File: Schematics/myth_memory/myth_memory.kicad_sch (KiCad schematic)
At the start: 6 parts, among them U1 74HC04, U3 SST39SF040, U4 74LS32, U5 74LS21, U6 4002, U94 KM62256CLP

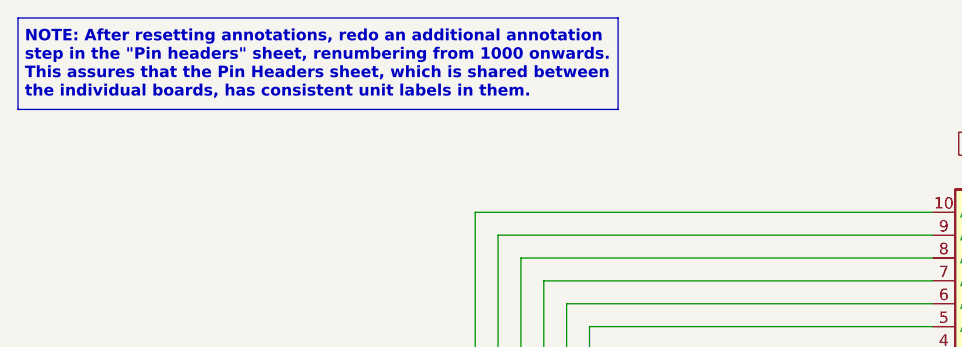
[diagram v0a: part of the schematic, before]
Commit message: Reduce number of shared headers
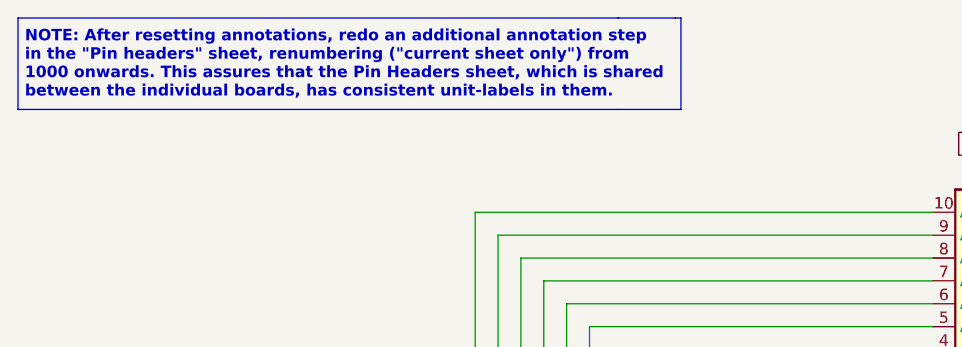
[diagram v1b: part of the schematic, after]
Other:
- note added: "NOTE: After resetting annotations, redo an additional annotation step in the "Pin headers" sheet, renumbering ("current sheet only") from 1000 onwards. This assures that the Pin Headers sheet, which is shared between the individual boards, has consistent unit-labels in them."
- note removed: "NOTE: After resetting annotations, redo an additional annotation step in the "Pin headers" sheet, renumbering from 1000 onwards. This assures that the Pin Headers sheet, which is shared between the individual boards, has consistent unit labels in them."

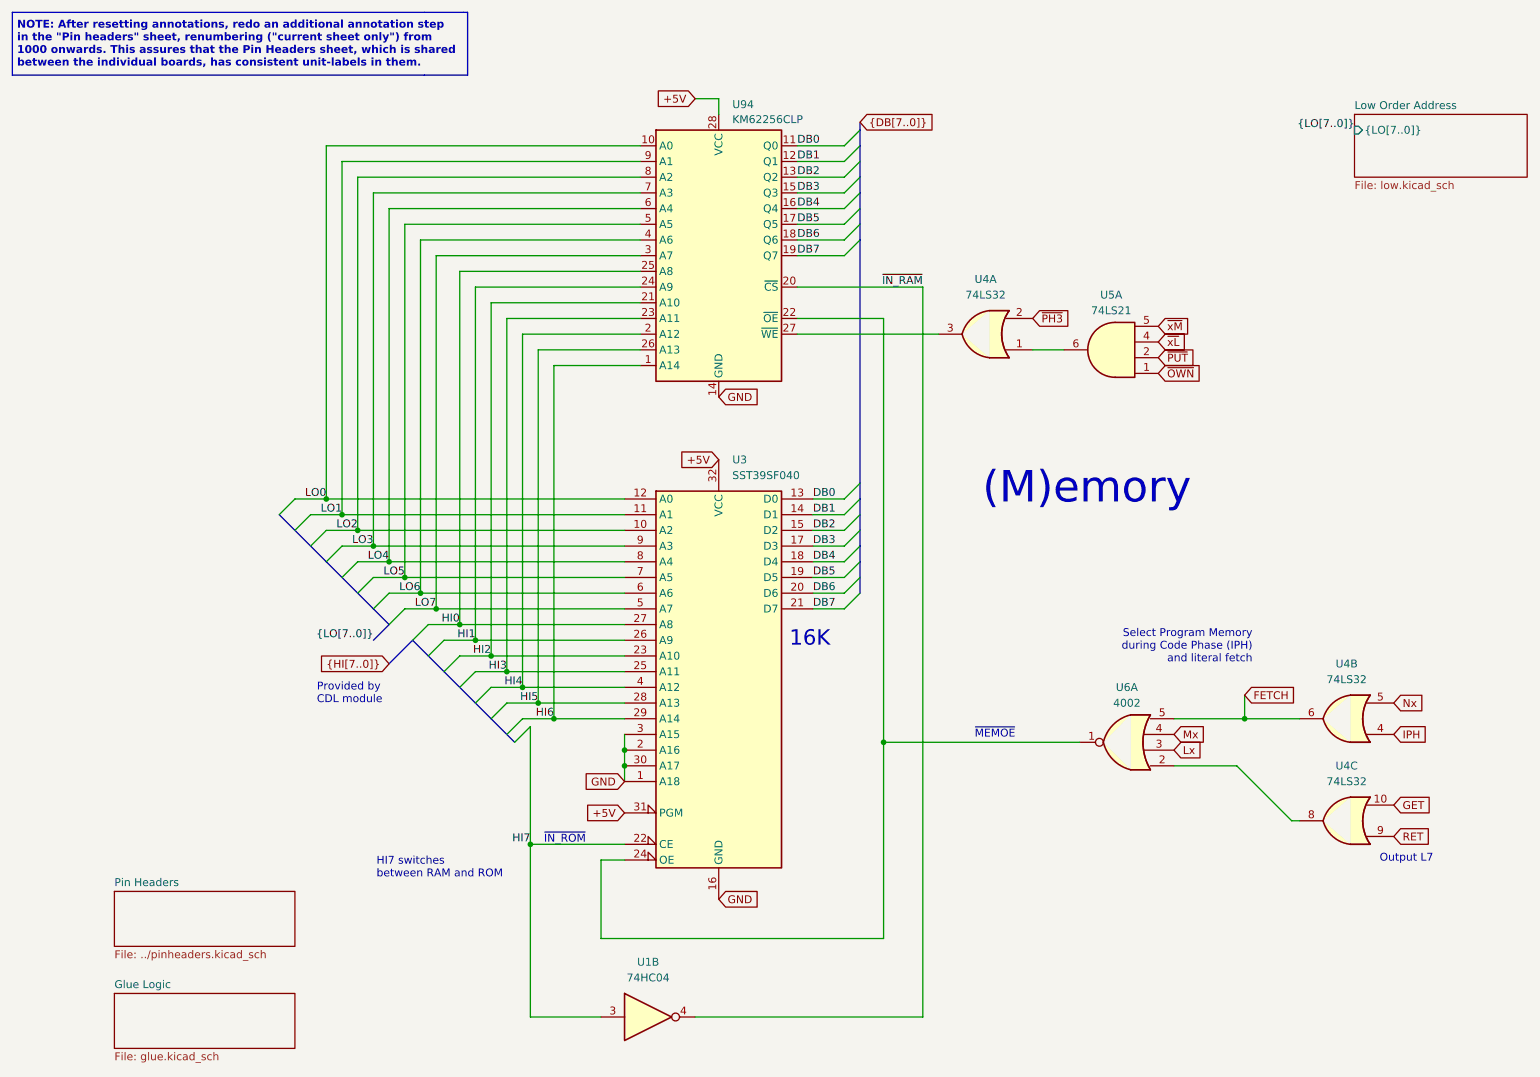
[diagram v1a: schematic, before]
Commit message: Improve schematics for readability
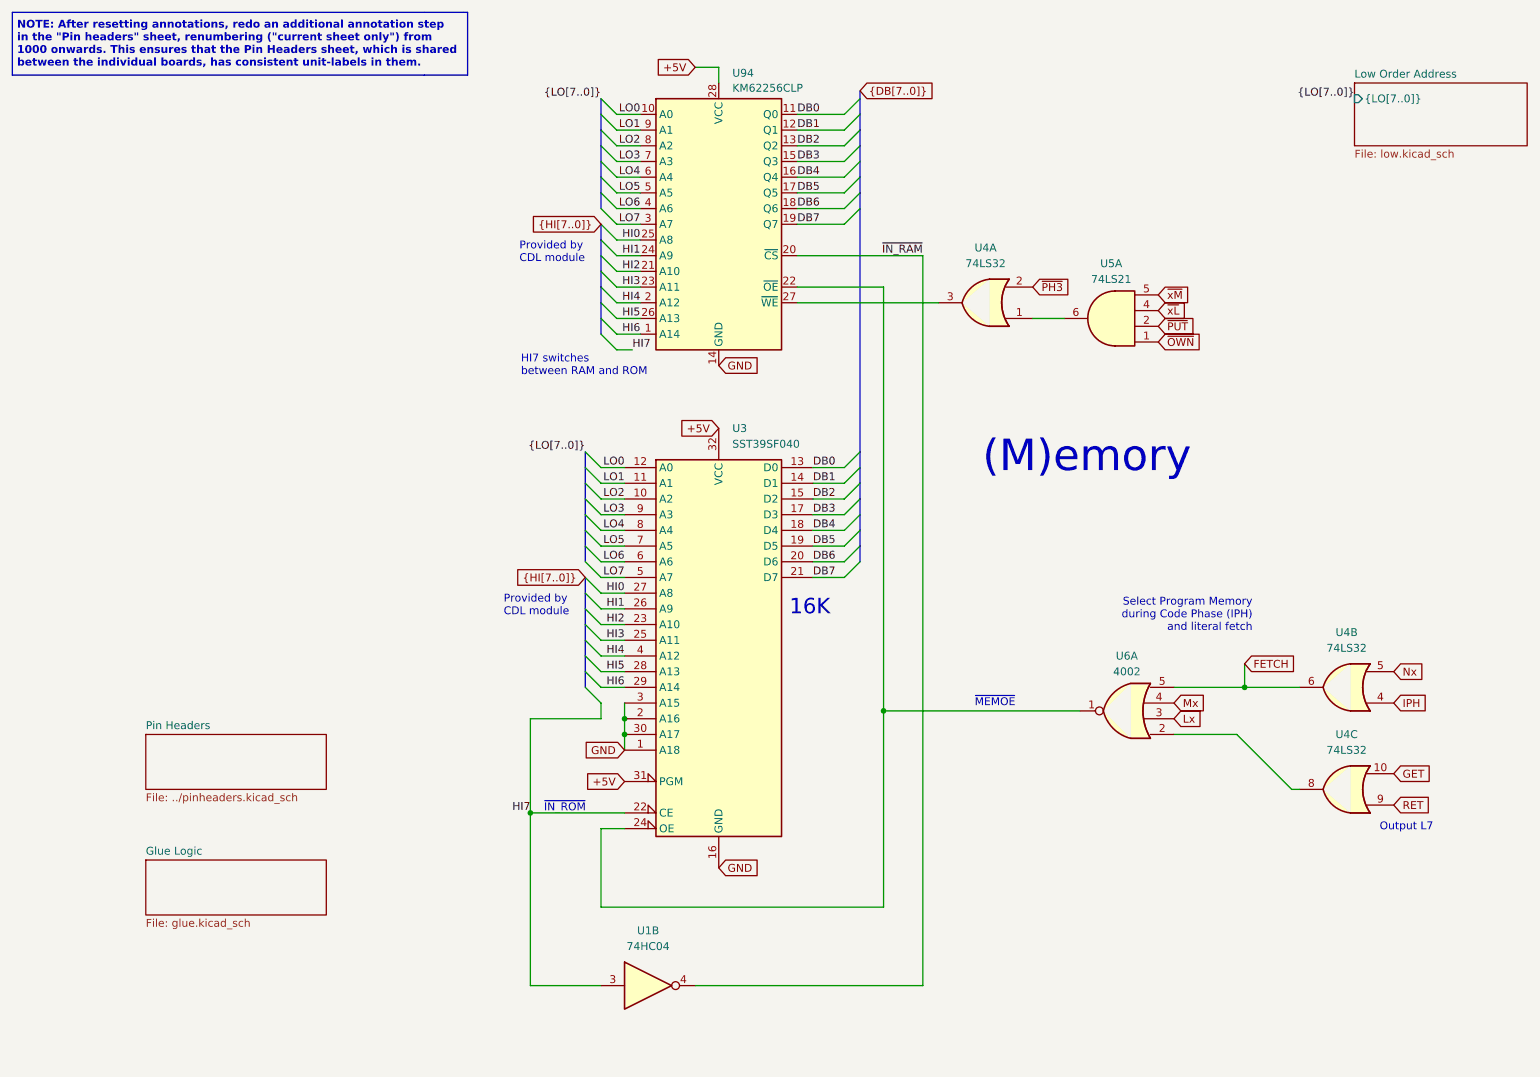
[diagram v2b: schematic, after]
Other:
- note added: "NOTE: After resetting annotations, redo an additional annotation step in the "Pin headers" sheet, renumbering ("current sheet only") from 1000 onwards. This ensures that the Pin Headers sheet, which is shared between the individual boards, has consistent unit-labels in them."
- note removed: "NOTE: After resetting annotations, redo an additional annotation step in the "Pin headers" sheet, renumbering ("current sheet only") from 1000 onwards. This assures that the Pin Headers sheet, which is shared between the individual boards, has consistent unit-labels in them."
- moved on the sheet: U1B, U3, U4A, U4B, U4C, U5A, U6A, U94

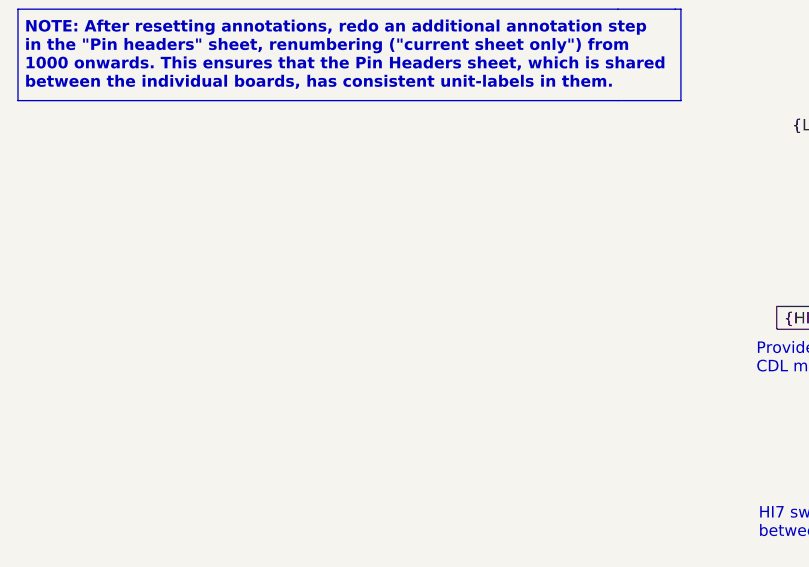
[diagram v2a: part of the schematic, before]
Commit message: Change d to g
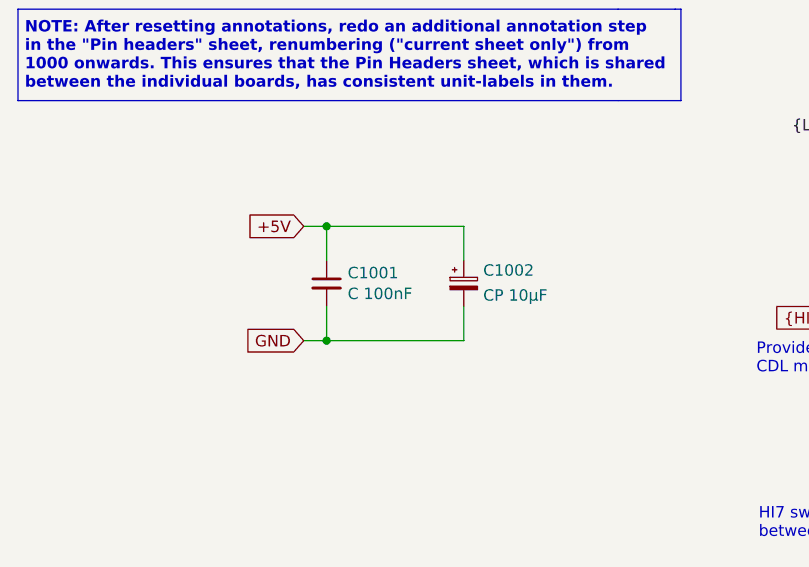
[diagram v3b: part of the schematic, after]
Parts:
- added C1001: C 100nF, Capacitor_THT:C_Disc_D5.0mm_W2.5mm_P2.50mm, symbol Device:C_Small
- added C1002: CP 10μF, Capacitor_THT:CP_Radial_D6.3mm_P2.50mm, symbol Device:C_Polarized_Small
- U1, U4, U5, U6: footprint (none) -> Package_DIP:DIP-14_W7.62mm_LongPads
- U3: footprint (none) -> Package_DIP:DIP-32_W15.24mm_LongPads
- U94: footprint Package_DIP:DIP-28_W15.24mm -> Package_DIP:DIP-28_W15.24mm_LongPads
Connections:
- net +5V: now also C1001.1, C1002.1
- net GND: now also C1001.2, C1002.2

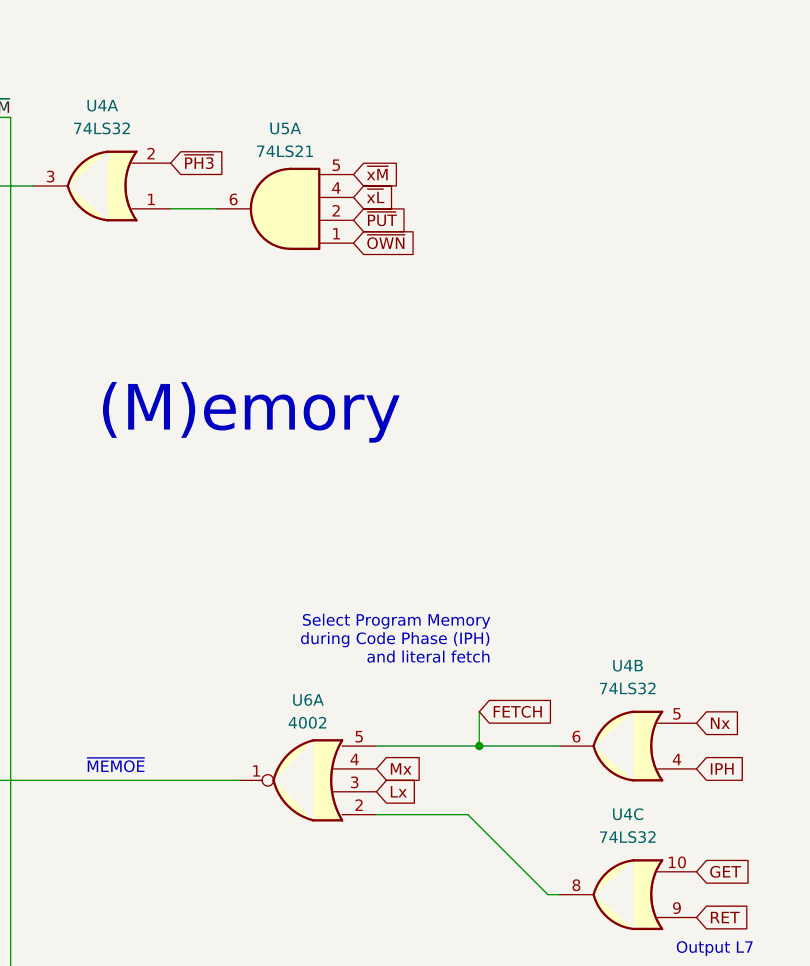
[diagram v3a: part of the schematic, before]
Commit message: Change semantics of xB
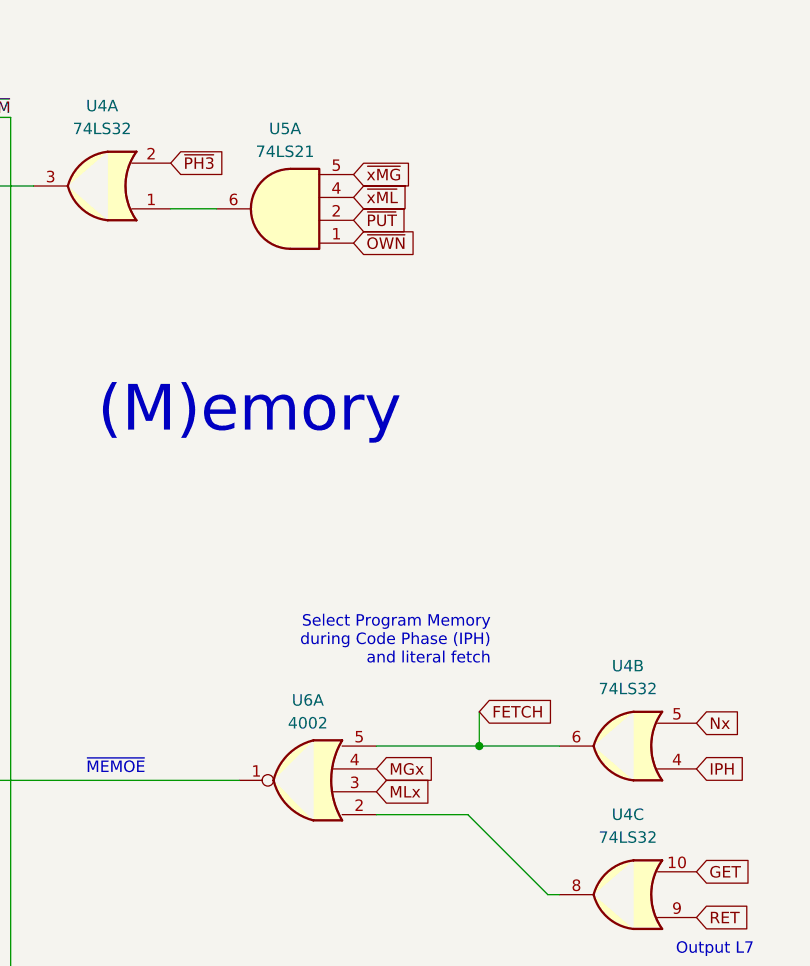
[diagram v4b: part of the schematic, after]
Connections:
- net Lx renamed MLx
- net Mx renamed MGx
- net ~{xL} renamed ~{xML}
- net ~{xM} renamed ~{xMG}
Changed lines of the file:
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@@
 		)
 	)
-	(global_label "~{xM}"
+	(global_label "~{xMG}"
 		(shape input)
 		(at 199.39 59.69 0)
@@
 		)
 		(property "Intersheetrefs" "${INTERSHEET_REFS}"
-			(at 204.8547 59.69 0)
+			(at 206.1247 59.69 0)
 			(effects
 				(font
@@
 		)
 	)
-	(global_label "Lx"
+	(global_label "MLx"
 		(shape input)
 		(at 201.93 128.27 0)
@@
 		)
 		(property "Intersheetrefs" "${INTERSHEET_REFS}"
-			(at 206.9714 128.27 0)
-			(effects
-				(font
-					(size 1.27 1.27)
-				)
-				(justify left)
-				(hide yes)
-			)
-		)
-	)
-	(global_label "~{xL}"
+			(at 208.4228 128.27 0)
+			(effects
+				(font
+					(size 1.27 1.27)
+				)
+				(justify left)
+				(hide yes)
+			)
+		)
+	)
+	(global_label "~{xML}"
 		(shape input)
 		(at 199.39 62.23 0)
@@
 		)
 		(property "Intersheetrefs" "${INTERSHEET_REFS}"
-			(at 204.4314 62.23 0)
+			(at 205.8828 62.23 0)
 			(effects
 				(font
@@
 		)
 	)
-	(global_label "Mx"
+	(global_label "MGx"
 		(shape input)
 		(at 201.93 125.73 0)
@@
 		)
 		(property "Intersheetrefs" "${INTERSHEET_REFS}"
-			(at 207.3947 125.73 0)
-			(effects
-				(font
+			(at 208.6647 125.73 0)
+			(effects
+				(font
